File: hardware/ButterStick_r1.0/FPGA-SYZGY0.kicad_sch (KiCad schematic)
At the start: 4 parts, among them U4 ECP5UM5G_85_CABGA381

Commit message: hw.r1d0: Update BOM fieids in schematic.
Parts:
- C157, C26: Mfg Samsung Electro-Mechanics -> Yageo; PN CL05B103KP5NNNC -> CC0402KRX5R6BB104; SN-DK 1276-1002-1-ND -> (none); Tol (none) -> 10V / X5R
- C25: Mfg Samsung Electro-Mechanics -> Yageo; PN CL05B104KP5NNNC -> CC0402KRX5R5BB474; SN-DK 1276-1002-1-ND -> (none)
- U4: Mfg (none) -> Lattice Semiconductor Corporation; PN (none) -> LFE5UM5G-85F-8BG381C; manf# ECP5UM5G_85 -> (none)
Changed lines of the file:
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@@
 (kicad_sch (version 20200618) (host eeschema "5.99.0-unknown-73168a9~101~ubuntu18.04.1")
-  (page 9 18)
+  (page 1 18)
   (paper "A4")
   (title_block
@@
       (effects (font (size 1.27 1.27)) hide)
     )
-    (property "SN-DK" "1276-1002-1-ND" (id 4) (at 29.21 241.3 0)
-      (effects (font (size 1.27 1.27)) hide)
-    )
-    (property "PN" "CL05B104KP5NNNC" (id 5) (at 29.21 241.3 0)
-      (effects (font (size 1.27 1.27)) hide)
-    )
-    (property "Mfg" "Samsung Electro-Mechanics" (id 6) (at 31.75 240.03 0)
+    (property "SN-DK" "" (id 4) (at 29.21 241.3 0)
+      (effects (font (size 1.27 1.27)) hide)
+    )
+    (property "PN" "CC0402KRX5R5BB474" (id 5) (at 29.21 241.3 0)
+      (effects (font (size 1.27 1.27)) hide)
+    )
+    (property "Mfg" "Yageo" (id 6) (at 31.75 240.03 0)
       (effects (font (size 1.27 1.27)) hide)
     )
@@
       (effects (font (size 1.27 1.27)) hide)
     )
-    (property "SN-DK" "1276-1002-1-ND" (id 4) (at 39.37 241.3 0)
-      (effects (font (size 1.27 1.27)) hide)
-    )
-    (property "PN" "CL05B103KP5NNNC" (id 5) (at 39.37 241.3 0)
-      (effects (font (size 1.27 1.27)) hide)
-    )
-    (property "Mfg" "Samsung Electro-Mechanics" (id 6) (at 31.75 240.03 0)
+    (property "SN-DK" "" (id 4) (at 39.37 241.3 0)
+      (effects (font (size 1.27 1.27)) hide)
+    )
+    (property "PN" "CC0402KRX5R6BB104" (id 5) (at 39.37 241.3 0)
+      (effects (font (size 1.27 1.27)) hide)
+    )
+    (property "Mfg" "Yageo" (id 6) (at 31.75 240.03 0)
+      (effects (font (size 1.27 1.27)) hide)
+    )
+    (property "Tol" "10V / X5R" (id 4) (at 189.23 64.77 0)
       (effects (font (size 1.27 1.27)) hide)
     )
@@
       (effects (font (size 1.27 1.27)) hide)
     )
-    (property "SN-DK" "1276-1002-1-ND" (id 4) (at 49.53 241.3 0)
-      (effects (font (size 1.27 1.27)) hide)
-    )
-    (property "PN" "CL05B103KP5NNNC" (id 5) (at 49.53 241.3 0)
-      (effects (font (size 1.27 1.27)) hide)
-    )
-    (property "Mfg" "Samsung Electro-Mechanics" (id 6) (at 41.91 240.03 0)
+    (property "SN-DK" "" (id 4) (at 49.53 241.3 0)
+      (effects (font (size 1.27 1.27)) hide)
+    )
+    (property "PN" "CC0402KRX5R6BB104" (id 5) (at 49.53 241.3 0)
+      (effects (font (size 1.27 1.27)) hide)
+    )
+    (property "Mfg" "Yageo" (id 6) (at 41.91 240.03 0)
+      (effects (font (size 1.27 1.27)) hide)
+    )
+    (property "Tol" "10V / X5R" (id 4) (at 199.39 64.77 0)
       (effects (font (size 1.27 1.27)) hide)
     )
@@
       (effects (font (size 1.524 1.524)) (justify right) hide)
     )
-    (property "manf#" "ECP5UM5G_85" (id 4) (at 135.89 69.85 0)
+    (property "manf#" "" (id 4) (at 135.89 69.85 0)
       (effects (font (size 1.524 1.524)) (justify right) hide)
     )
-  )
+    (property "Mfg" "Lattice Semiconductor Corporation" (id 4) (at 132.08 68.58 0)
+      (effects (font (size 1.27 1.27)) hide)
+    )
+    (property "PN" "LFE5UM5G-85F-8BG381C" (id 5) (at 132.08 68.58 0)
+      (effects (font (size 1.27 1.27)) hide)
+    )
+  )

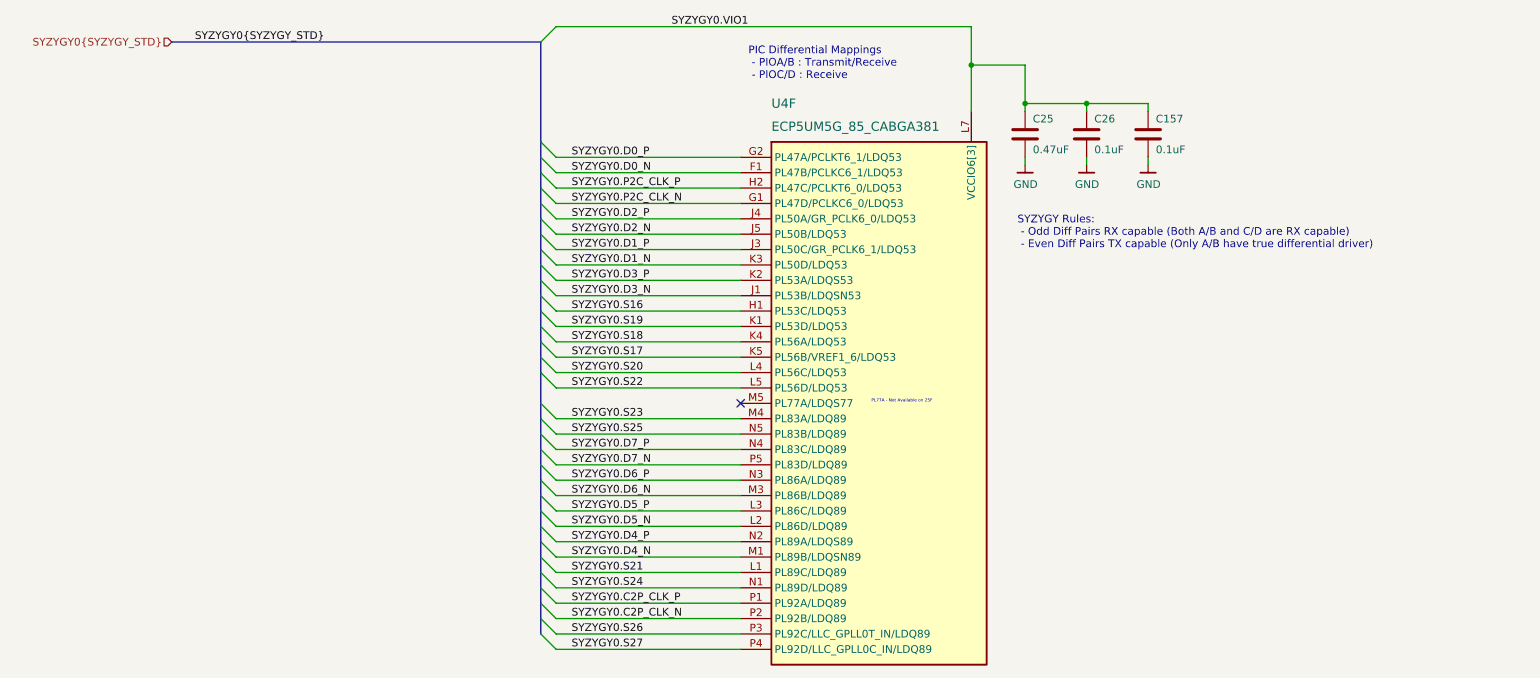
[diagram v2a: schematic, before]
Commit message: hw.r1d0: Fix RGMII straps
This commit correctly sets the stop resistos on the RGMII lines to 1K5
instead of DNP.
Also regenerate and add a schematic in PDF format.

Fixes #6
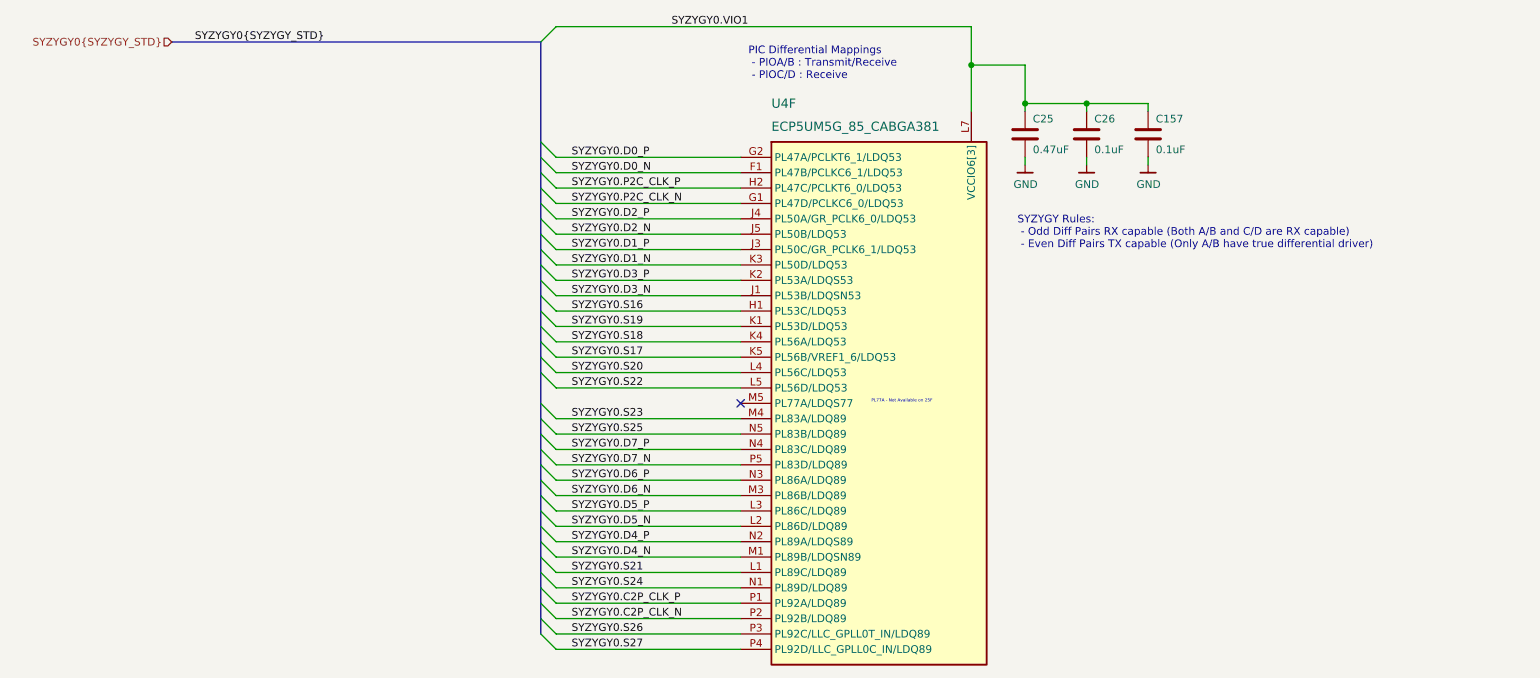
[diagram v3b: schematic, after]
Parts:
- U4: PN LFE5UM5G-85F-8BG381C -> LFE5UM5G-85F-8BG381I
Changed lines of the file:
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@@
-(kicad_sch (version 20200618) (host eeschema "5.99.0-unknown-73168a9~101~ubuntu18.04.1")
+(kicad_sch (version 20201015) (generator eeschema)
   (page 1 18)
   (paper "A4")
   (title_block
     (title "ButterStick")
-    (date "2020-07-17")
+    (date "2020-11-01")
     (rev "r1.0")
     (company "GsD")
     (comment 1 "Functional prototyping board for the Lattice ECP5.")
-  )
-  (junction (at 170.18 53.34) (diameter 0) (color 0 0 0 0))
-  (junction (at 179.07 59.69) (diameter 0) (color 0 0 0 0))
-  (junction (at 189.23 59.69) (diameter 0) (color 0 0 0 0))
+    (comment 2 "SYZYGY compatible")
+  )
+  (junction (at 170.18 53.34) (diameter 1.016) (color 0 0 0 0))
+  (junction (at 179.07 59.69) (diameter 1.016) (color 0 0 0 0))
+  (junction (at 189.23 59.69) (diameter 1.016) (color 0 0 0 0))
   (no_connect (at 132.08 109.22))
   (bus_entry (at 99.06 49.53) (size 2.54 -2.54)
@@
     (stroke (width 0) (type solid) (color 0 0 0 0))
   )
-  (bus (pts (xy 99.06 66.04) (xy 99.06 71.12))
+  (bus (pts (xy 99.06 66.04) (xy 99.06 68.58))
+    (stroke (width 0) (type solid) (color 0 0 0 0))
+  )
+  (bus (pts (xy 99.06 68.58) (xy 99.06 71.12))
     (stroke (width 0) (type solid) (color 0 0 0 0))
   )
@@
     (stroke (width 0) (type solid) (color 0 0 0 0))
   )
-  (bus (pts (xy 99.06 73.66) (xy 99.06 78.74))
-    (stroke (width 0) (type solid) (color 0 0 0 0))
-  )
-  (bus (pts (xy 99.06 78.74) (xy 99.06 83.82))
-    (stroke (width 0) (type solid) (color 0 0 0 0))
-  )
-  (bus (pts (xy 99.06 83.82) (xy 99.06 88.9))
-    (stroke (width 0) (type solid) (color 0 0 0 0))
-  )
-  (bus (pts (xy 99.06 88.9) (xy 99.06 93.98))
-    (stroke (width 0) (type solid) (color 0 0 0 0))
-  )
-  (bus (pts (xy 99.06 93.98) (xy 99.06 99.06))
-    (stroke (width 0) (type solid) (color 0 0 0 0))
-  )
-  (bus (pts (xy 99.06 99.06) (xy 99.06 104.14))
-    (stroke (width 0) (type solid) (color 0 0 0 0))
-  )
-  (bus (pts (xy 99.06 104.14) (xy 99.06 111.76))
-    (stroke (width 0) (type solid) (color 0 0 0 0))
-  )
-  (bus (pts (xy 99.06 111.76) (xy 99.06 116.84))
-    (stroke (width 0) (type solid) (color 0 0 0 0))
-  )
-  (bus (pts (xy 99.06 116.84) (xy 99.06 121.92))
-    (stroke (width 0) (type solid) (color 0 0 0 0))
-  )
-  (bus (pts (xy 99.06 121.92) (xy 99.06 127))
-    (stroke (width 0) (type solid) (color 0 0 0 0))
-  )
-  (bus (pts (xy 99.06 127) (xy 99.06 132.08))
-    (stroke (width 0) (type solid) (color 0 0 0 0))
-  )
-  (bus (pts (xy 99.06 132.08) (xy 99.06 137.16))
-    (stroke (width 0) (type solid) (color 0 0 0 0))
-  )
-  (bus (pts (xy 99.06 137.16) (xy 99.06 142.24))
-    (stroke (width 0) (type solid) (color 0 0 0 0))
-  )
-  (bus (pts (xy 99.06 142.24) (xy 99.06 147.32))
+  (bus (pts (xy 99.06 73.66) (xy 99.06 76.2))
+    (stroke (width 0) (type solid) (color 0 0 0 0))
+  )
+  (bus (pts (xy 99.06 76.2) (xy 99.06 78.74))
+    (stroke (width 0) (type solid) (color 0 0 0 0))
+  )
+  (bus (pts (xy 99.06 78.74) (xy 99.06 81.28))
+    (stroke (width 0) (type solid) (color 0 0 0 0))
+  )
+  (bus (pts (xy 99.06 81.28) (xy 99.06 83.82))
+    (stroke (width 0) (type solid) (color 0 0 0 0))
+  )
+  (bus (pts (xy 99.06 83.82) (xy 99.06 86.36))
+    (stroke (width 0) (type solid) (color 0 0 0 0))
+  )
+  (bus (pts (xy 99.06 86.36) (xy 99.06 88.9))
+    (stroke (width 0) (type solid) (color 0 0 0 0))
+  )
+  (bus (pts (xy 99.06 88.9) (xy 99.06 91.44))
+    (stroke (width 0) (type solid) (color 0 0 0 0))
+  )
+  (bus (pts (xy 99.06 91.44) (xy 99.06 93.98))
+    (stroke (width 0) (type solid) (color 0 0 0 0))
+  )
+  (bus (pts (xy 99.06 93.98) (xy 99.06 96.52))
+    (stroke (width 0) (type solid) (color 0 0 0 0))
+  )
+  (bus (pts (xy 99.06 96.52) (xy 99.06 99.06))
+    (stroke (width 0) (type solid) (color 0 0 0 0))
+  )
+  (bus (pts (xy 99.06 99.06) (xy 99.06 101.6))
+    (stroke (width 0) (type solid) (color 0 0 0 0))
+  )
+  (bus (pts (xy 99.06 101.6) (xy 99.06 104.14))
+    (stroke (width 0) (type solid) (color 0 0 0 0))
+  )
+  (bus (pts (xy 99.06 104.14) (xy 99.06 109.22))
+    (stroke (width 0) (type solid) (color 0 0 0 0))
+  )
+  (bus (pts (xy 99.06 109.22) (xy 99.06 111.76))
+    (stroke (width 0) (type solid) (color 0 0 0 0))
+  )
+  (bus (pts (xy 99.06 111.76) (xy 99.06 114.3))
+    (stroke (width 0) (type solid) (color 0 0 0 0))
+  )
+  (bus (pts (xy 99.06 114.3) (xy 99.06 116.84))
+    (stroke (width 0) (type solid) (color 0 0 0 0))
+  )
+  (bus (pts (xy 99.06 116.84) (xy 99.06 119.38))
+    (stroke (width 0) (type solid) (color 0 0 0 0))
+  )
+  (bus (pts (xy 99.06 119.38) (xy 99.06 121.92))
+    (stroke (width 0) (type solid) (color 0 0 0 0))
+  )
+  (bus (pts (xy 99.06 121.92) (xy 99.06 124.46))
+    (stroke (width 0) (type solid) (color 0 0 0 0))
+  )
+  (bus (pts (xy 99.06 124.46) (xy 99.06 127))
+    (stroke (width 0) (type solid) (color 0 0 0 0))
+  )
+  (bus (pts (xy 99.06 127) (xy 99.06 129.54))
+    (stroke (width 0) (type solid) (color 0 0 0 0))
+  )
+  (bus (pts (xy 99.06 129.54) (xy 99.06 132.08))
+    (stroke (width 0) (type solid) (color 0 0 0 0))
+  )
+  (bus (pts (xy 99.06 132.08) (xy 99.06 134.62))
+    (stroke (width 0) (type solid) (color 0 0 0 0))
+  )
+  (bus (pts (xy 99.06 134.62) (xy 99.06 137.16))
+    (stroke (width 0) (type solid) (color 0 0 0 0))
+  )
+  (bus (pts (xy 99.06 137.16) (xy 99.06 139.7))
+    (stroke (width 0) (type solid) (color 0 0 0 0))
+  )
+  (bus (pts (xy 99.06 139.7) (xy 99.06 142.24))
+    (stroke (width 0) (type solid) (color 0 0 0 0))
+  )
+  (bus (pts (xy 99.06 142.24) (xy 99.06 144.78))
+    (stroke (width 0) (type solid) (color 0 0 0 0))
+  )
+  (bus (pts (xy 99.06 144.78) (xy 99.06 147.32))
     (stroke (width 0) (type solid) (color 0 0 0 0))
   )
@@
       (effects (font (size 1.524 1.524)) (justify right) hide)
     )
+    (property "PN" "LFE5UM5G-85F-8BG381I" (id 5) (at 132.08 68.58 0)
+      (effects (font (size 1.27 1.27)) hide)
+    )
     (property "Mfg" "Lattice Semiconductor Corporation" (id 4) (at 132.08 68.58 0)
       (effects (font (size 1.27 1.27)) hide)
     )
-    (property "PN" "LFE5UM5G-85F-8BG381C" (id 5) (at 132.08 68.58 0)
-      (effects (font (size 1.27 1.27)) hide)
-    )
